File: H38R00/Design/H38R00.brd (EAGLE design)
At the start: 34.6 x 60 mm, 77 parts, among them P1 HEXABIT_17.32_X2_POWER_ONLY, U1 LM5160DNT, U2 TPS65130RGERT, U3 TPS76433DBVT

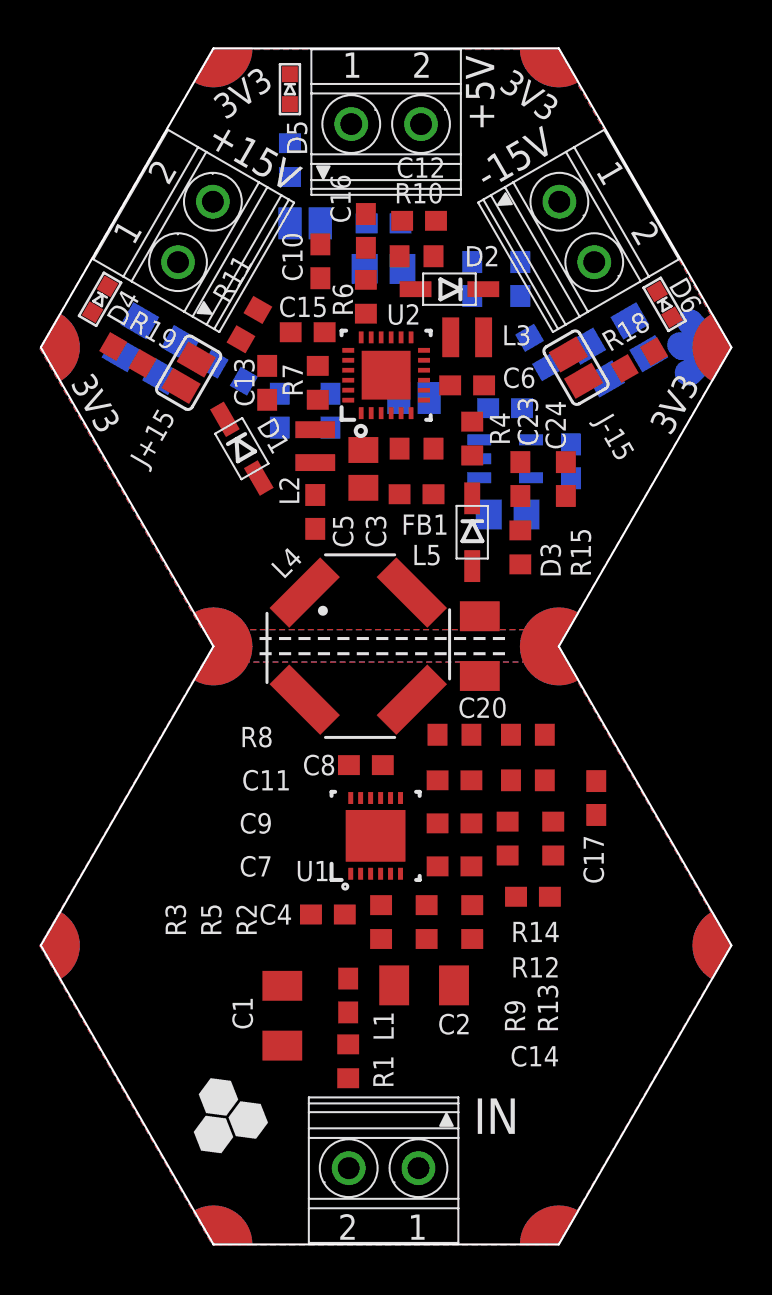
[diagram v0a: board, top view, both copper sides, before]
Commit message: Route most of top layer and raarrange some components
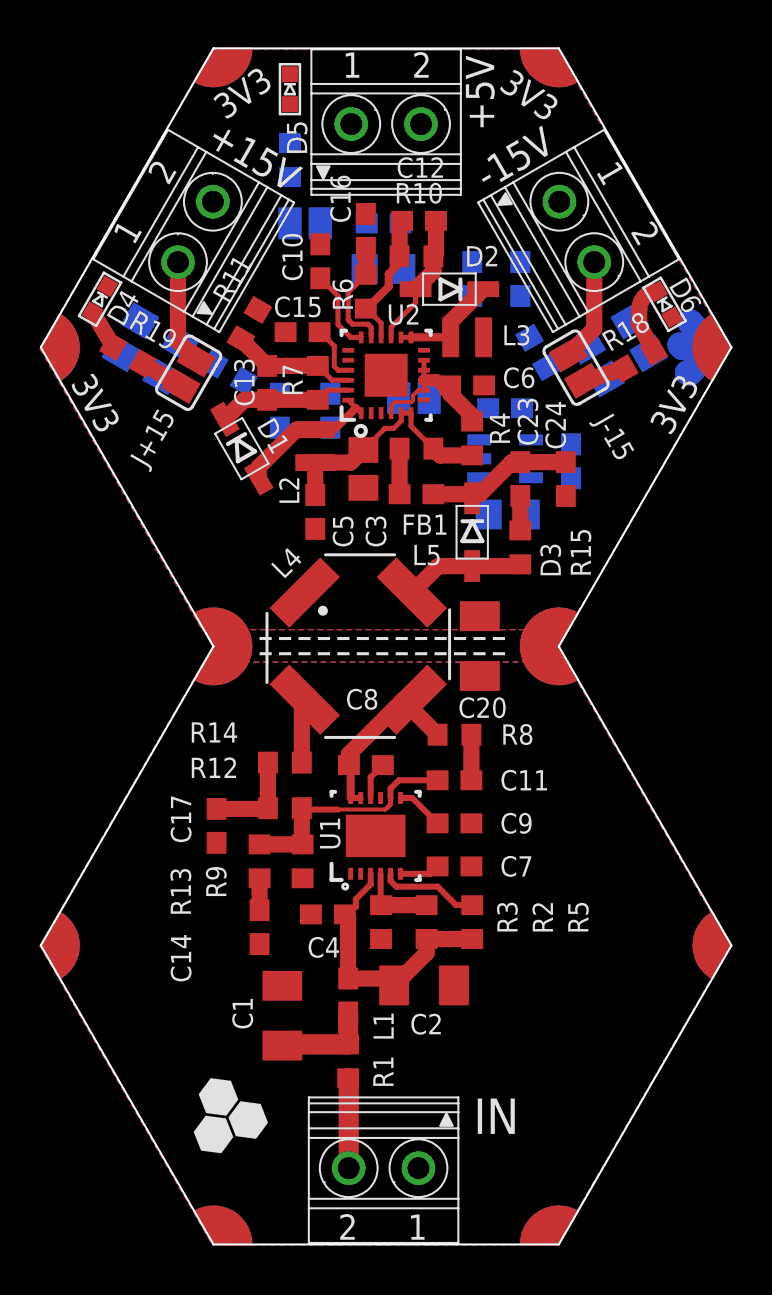
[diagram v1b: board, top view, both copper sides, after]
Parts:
- moved C17 19.1 mm to (24.5, 40.5)
- moved R13 14.8 mm to (26.7, 38.7)
- moved C14 13.8 mm to (26.7, 35.4), turned to 270 degrees
- moved R12 12.3 mm to (27.9, 41.4), turned to 180 degrees
- moved R14 12.3 mm to (27.9, 43.7), turned to 0 degrees
- moved R9 10.4 mm to (28.8, 38.7)
- moved R6 0.25 mm to (32.0, 67.3)
- moved C15 0.25 mm to (28.8, 65.3)
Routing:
- net N$3: track 0.00 -> 13.7 mm
- net N$18: track 0.00 -> 12.0 mm
- net N$10: track 0.00 -> 11.9 mm
- net N$7: track 0.00 -> 9.49 mm
- net N$23: track 0.00 -> 7.86 mm
- net N$15: track 0.00 -> 7.60 mm
- net N$21: track 0.00 -> 7.57 mm
- net N$22: track 0.00 -> 6.79 mm
- net N$27: track 0.00 -> 6.78 mm
- net N$28: track 0.00 -> 6.56 mm
- net N$30: track 0.00 -> 6.25 mm
- net N$16: track 0.00 -> 6.03 mm
- net N$29: track 0.00 -> 5.79 mm
- net N$26: track 0.00 -> 5.58 mm
- net +15V: track 0.00 -> 5.27 mm
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
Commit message: Via stitching. Ready for DRC
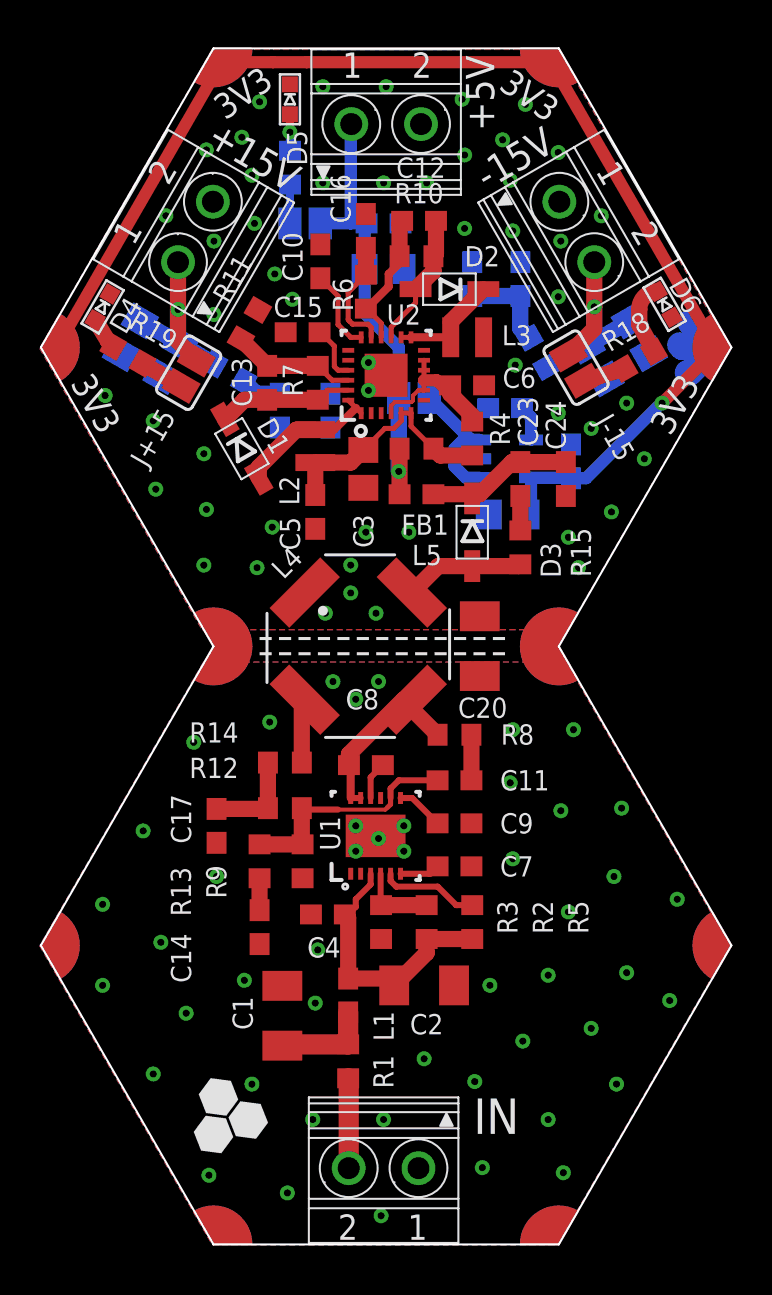
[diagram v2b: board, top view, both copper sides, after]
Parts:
- moved D5 0.51 mm to (28.2, 77.0)
- moved D4 0.40 mm to (18.8, 66.5)
- moved R20 0.38 mm to (28.2, 73.5)
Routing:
- net +3V3: track 0.00 -> 63.5 mm, vias 0 -> 1
- net +5V: track 2.29 -> 22.8 mm, vias 0 -> 1
- net N$36: track 0.00 -> 7.17 mm
- net -15V: track 5.17 -> 12.1 mm, vias 0 -> 1
- net +15V: track 5.27 -> 11.4 mm, vias 0 -> 1
- net N$27: track 6.78 -> 11.5 mm
- net N$22: track 6.79 -> 8.86 mm
- net N$19: track 0.00 -> 1.94 mm
- net N$20: track 0.00 -> 1.83 mm, vias 0 -> 1
- net N$35: track 0.00 -> 1.78 mm
- net IGND: vias 0 -> 50

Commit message: DRC OK
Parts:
- moved C8 0.92 mm to (31.1, 43.8)
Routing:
- net IGND: track 5.58 -> 0.00 mm
- net N$9: track 2.38 -> 6.34 mm, vias 0 -> 2
- net N$22: track 8.86 -> 11.6 mm, vias 0 -> 1
- net N$27: track 11.5 -> 13.9 mm, vias 0 -> 1
- net N$7: track 9.49 -> 11.1 mm
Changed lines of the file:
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@@
 <attribute name="VAULT_REVISION" value="AD34EA21-00F0-458B-A44F-F680A14C5CDA" x="31.623" y="49.53" size="1.778" layer="27" rot="R45" display="off"/>
 </element>
-<element name="C8" library="Hexabitz" package="C-0603" value="10nF" x="32.004" y="43.561" smashed="yes" rot="R180">
-<attribute name="CAPACITANCE" value="10nF" x="32.004" y="43.561" size="1.778" layer="27" rot="R180" display="off"/>
-<attribute name="MFN" value="KEMET" x="32.004" y="43.561" size="1.778" layer="27" rot="R180" display="off"/>
-<attribute name="MPN" value="C0603C103J5RACTU" x="32.004" y="43.561" size="1.778" layer="27" rot="R180" display="off"/>
-<attribute name="NAME" x="30.988" y="46.355" size="1.016" layer="25"/>
-<attribute name="OCTOPART_URL" value="https://octopart.com/c0603c103j5ractu-kemet-91371?r=sp&amp;s=Kyc2xDn-SuWGmNLJldLSIQ" x="32.004" y="43.561" size="1.778" layer="27" rot="R180" display="off"/>
-<attribute name="TOLERANCE" value="10%" x="32.004" y="43.561" size="1.778" layer="27" rot="R180" display="off"/>
-<attribute name="VALUE" x="32.639" y="45.466" size="1.016" layer="27" rot="R180"/>
-<attribute name="VOLTAGE_RATING" value="50V" x="32.004" y="43.561" size="1.778" layer="27" rot="R180" display="off"/>
+<element name="C8" library="Hexabitz" package="C-0603" value="10nF" x="31.115" y="43.815" smashed="yes" rot="R180">
+<attribute name="CAPACITANCE" value="10nF" x="31.115" y="43.815" size="1.778" layer="27" rot="R180" display="off"/>
+<attribute name="MFN" value="KEMET" x="31.115" y="43.815" size="1.778" layer="27" rot="R180" display="off"/>
+<attribute name="MPN" value="C0603C103J5RACTU" x="31.115" y="43.815" size="1.778" layer="27" rot="R180" display="off"/>
+<attribute name="NAME" x="30.099" y="46.609" size="1.016" layer="25"/>
+<attribute name="OCTOPART_URL" value="https://octopart.com/c0603c103j5ractu-kemet-91371?r=sp&amp;s=Kyc2xDn-SuWGmNLJldLSIQ" x="31.115" y="43.815" size="1.778" layer="27" rot="R180" display="off"/>
+<attribute name="TOLERANCE" value="10%" x="31.115" y="43.815" size="1.778" layer="27" rot="R180" display="off"/>
+<attribute name="VALUE" x="31.75" y="45.72" size="1.016" layer="27" rot="R180"/>
+<attribute name="VOLTAGE_RATING" value="50V" x="31.115" y="43.815" size="1.778" layer="27" rot="R180" display="off"/>
 </element>
 <element name="C9" library="Hexabitz" package="C-0603" value="1uF" x="36.449" y="40.64" smashed="yes">
@@
 <vertex x="15.64919375" y="64.4652"/>
 </polygon>
-<polygon width="0.1016" layer="16">
-<vertex x="49.784" y="65.151"/>
-<vertex x="49.784" y="64.262"/>
-<vertex x="49.784" y="63.754"/>
-</polygon>
 <contactref element="P1" pad="PAD_PD12"/>
-<wire x1="49.54" y1="64.516" x2="47.879" y2="64.516" width="1.27" layer="16"/>
-<wire x1="47.879" y1="64.516" x2="47.752" y2="64.643" width="1.27" layer="16"/>
-<wire x1="49.54" y1="64.516" x2="48.27" y2="65.786" width="1.27" layer="16"/>
-<wire x1="48.27" y1="65.786" x2="48.26" y2="65.786" width="1.27" layer="16"/>
-<wire x1="49.54" y1="64.516" x2="48.27" y2="63.246" width="1.27" layer="16"/>
-<wire x1="48.27" y1="63.246" x2="48.133" y2="63.246" width="1.27" layer="16"/>
 <via x="24.003" y="74.422" extent="1-16" drill="0.35"/>
 <via x="25.781" y="75.057" extent="1-16" drill="0.35"/>
@@
 <contactref element="R8" pad="1"/>
 <contactref element="L4" pad="3"/>
-<wire x1="31.242" y1="43.473" x2="31.154" y2="43.561" width="0.8128" layer="1"/>
-<wire x1="31.154" y1="43.561" x2="31.154" y2="44.108" width="0.8128" layer="1"/>
+<wire x1="31.242" y1="42.584" x2="30.265" y2="43.561" width="0.4064" layer="1"/>
+<wire x1="30.265" y1="43.561" x2="30.265" y2="43.815" width="0.4064" layer="1"/>
 <wire x1="33.88899375" y1="46.84299375" x2="34.310003125" y2="46.84299375" width="0.8128" layer="1"/>
-<wire x1="31.154" y1="44.108" x2="33.88899375" y2="46.84299375" width="0.8128" layer="1"/>
-<wire x1="35.599" y1="45.085" x2="33.88899375" y2="46.79500625" width="0.8128" layer="1"/>
-<wire x1="33.88899375" y1="46.79500625" x2="33.88899375" y2="46.84299375" width="0.8128" layer="1"/>
+<wire x1="30.265" y1="44.235" x2="31.72999375" y2="45.69999375" width="0.8128" layer="1"/>
+<wire x1="30.265" y1="43.815" x2="30.265" y2="44.235" width="0.8128" layer="1"/>
 <wire x1="31.742" y1="41.91" x2="31.242" y2="41.91" width="0.3048" layer="1"/>
-<wire x1="31.242" y1="41.91" x2="31.242" y2="43.473" width="0.4064" layer="1"/>
+<wire x1="31.242" y1="41.91" x2="31.242" y2="42.584" width="0.4064" layer="1"/>
+<wire x1="31.72999375" y1="45.69999375" x2="33.167003125" y2="45.69999375" width="0.8128" layer="1"/>
+<wire x1="33.167003125" y1="45.69999375" x2="34.310003125" y2="46.84299375" width="0.8128" layer="1"/>
+<wire x1="34.310003125" y1="46.373996875" x2="34.310003125" y2="46.84299375" width="0.8128" layer="1"/>
+<wire x1="35.599" y1="45.085" x2="34.310003125" y2="46.373996875" width="0.8128" layer="1"/>
 </signal>
 <signal name="N$8">
 <contactref element="U1" pad="10"/>
 <contactref element="C8" pad="1"/>
-<wire x1="32.241996875" y1="41.91" x2="32.241996875" y2="42.948996875" width="0.3048" layer="1"/>
-<wire x1="32.241996875" y1="42.948996875" x2="32.854" y2="43.561" width="0.3048" layer="1"/>
+<wire x1="32.241996875" y1="41.91" x2="32.241996875" y2="43.538003125" width="0.3048" layer="1"/>
+<wire x1="32.241996875" y1="43.538003125" x2="31.965" y2="43.815" width="0.3048" layer="1"/>
 </signal>
 <signal name="N$9">
@@
 <wire x1="33.742" y1="41.91" x2="34.329" y2="41.91" width="0.3048" layer="1"/>
 <wire x1="34.329" y1="41.91" x2="35.599" y2="40.64" width="0.3048" layer="1"/>
-<wire x1="32.742" y1="41.91" x2="33.742" y2="41.91" width="0" layer="19" extent="1-1"/>
+<wire x1="32.742" y1="41.91" x2="32.742" y2="42.775" width="0.254" layer="1"/>
+<wire x1="32.742" y1="42.775" x2="33.528" y2="43.561" width="0.254" layer="1"/>
+<via x="33.528" y="43.561" extent="1-16" drill="0.35"/>
+<wire x1="33.528" y1="43.561" x2="34.329" y2="42.76" width="0.254" layer="16"/>
+<wire x1="34.329" y1="42.76" x2="34.329" y2="41.91" width="0.254" layer="16"/>
+<via x="34.329" y="41.91" extent="1-16" drill="0.35"/>
 </signal>
 <signal name="N$10">
@@
 <wire x1="24.931" y1="60.908240625" x2="25.910759375" y2="61.888" width="0.8128" layer="1"/>
 <wire x1="25.910759375" y1="61.888" x2="27.051" y2="61.888" width="0.8128" layer="1"/>
-<wire x1="27.051" y1="61.888" x2="29.591" y2="61.888" width="0.8128" layer="1"/>
+<wire x1="29.337" y1="62.142" x2="28.575" y2="62.142" width="0.8128" layer="1"/>
+<wire x1="28.575" y1="62.142" x2="27.305" y2="62.142" width="0.8128" layer="1"/>
+<wire x1="27.051" y1="61.888" x2="27.305" y2="62.142" width="0.8128" layer="1"/>
+<wire x1="29.337" y1="62.142" x2="29.591" y2="61.888" width="0.8128" layer="1"/>
 <wire x1="31.12" y1="62.369" x2="30.072" y2="62.369" width="0.254" layer="1"/>
 <wire x1="30.072" y1="62.369" x2="29.591" y2="61.888" width="0.254" layer="1"/>
 <wire x1="25.882121875" y1="62.821" x2="26.512121875" y2="62.191" width="0.8128" layer="16"/>
 <wire x1="26.512121875" y1="62.191" x2="27.686" y2="62.191" width="0.8128" layer="16"/>
-<wire x1="30.072" y1="62.369" x2="30.226" y2="62.191" width="0" layer="19" extent="1-16"/>
-<wire x1="26.512121875" y1="62.191" x2="27.051" y2="61.888" width="0" layer="19" extent="1-16"/>
+<wire x1="27.686" y1="62.191" x2="28.526" y2="62.191" width="0.8128" layer="16"/>
+<wire x1="28.526" y1="62.191" x2="28.575" y2="62.142" width="0.8128" layer="16"/>
+<via x="28.575" y="62.142" extent="1-16" drill="0.35"/>
+<wire x1="28.575" y1="62.142" x2="30.177" y2="62.142" width="0.8128" layer="16"/>
+<wire x1="30.177" y1="62.142" x2="30.226" y2="62.191" width="0.8128" layer="16"/>
 </signal>
 <signal name="N$23">
@@
 <wire x1="39.751" y1="67.095" x2="39.751" y2="65.46211875" width="0.8128" layer="16"/>
 <wire x1="39.751" y1="65.46211875" x2="40.215" y2="64.99811875" width="0.8128" layer="16"/>
-<wire x1="35.394" y1="68.336" x2="37.338" y2="67.095" width="0" layer="19" extent="1-16"/>
+<wire x1="37.338" y1="67.095" x2="36.635" y2="67.095" width="0.6096" layer="16"/>
+<wire x1="36.635" y1="67.095" x2="35.394" y2="68.336" width="0.6096" layer="16"/>
+<via x="35.394" y="68.336" extent="1-16" drill="0.35"/>
 </signal>
 <signal name="+5V">
@@
 <contactref element="FB1" pad="1"/>
 <contactref element="J3V3" pad="2"/>
-<wire x1="33.694" y1="59.436" x2="33.694" y2="57.15" width="0.8128" layer="1"/>
 <wire x1="33.655" y1="61.976" x2="33.655" y2="64.516" width="0.6096" layer="16"/>
 <wire x1="31.943" y1="66.228" x2="31.943" y2="68.453" width="0.6096" layer="16"/>
@@
 <wire x1="33.655" y1="61.976" x2="33.655" y2="58.293" width="0.8128" layer="16"/>
 <via x="33.655" y="58.293" extent="1-16" drill="0.35"/>
-<wire x1="33.655" y1="58.293" x2="33.694" y2="59.436" width="0" layer="19" extent="1-16"/>
+<wire x1="33.694" y1="57.15" x2="33.694" y2="58.254" width="0.8128" layer="1"/>
+<wire x1="33.694" y1="58.254" x2="33.655" y2="58.293" width="0.8128" layer="1"/>
+<wire x1="33.655" y1="58.293" x2="33.655" y2="59.397" width="0.8128" layer="1"/>
+<wire x1="33.655" y1="59.397" x2="33.694" y2="59.436" width="0.8128" layer="1"/>
 </signal>
 <signal name="+15V">
@@
 <wire x1="33.694" y1="69.088" x2="33.694" y2="68.746" width="0.4064" layer="1"/>
 <wire x1="33.694" y1="68.746" x2="33.147" y2="68.199" width="0.4064" layer="1"/>
-<wire x1="32.77" y1="65.019" x2="32.77" y2="65.733" width="0.254" layer="1"/>
-<wire x1="32.77" y1="65.733" x2="32.297" y2="66.206" width="0.254" layer="1"/>
-<wire x1="32.297" y1="66.206" x2="32.043" y2="66.46" width="0" layer="19" extent="1-1"/>
+<wire x1="32.77" y1="65.821" x2="32.131" y2="66.46" width="0.254" layer="1"/>
+<wire x1="32.004" y1="66.46" x2="32.131" y2="66.46" width="0.254" layer="1"/>
+<wire x1="32.77" y1="65.019" x2="32.77" y2="65.821" width="0.254" layer="1"/>
 </signal>
 <signal name="N$29">
@@
 <mfgpreviewcolor name="substratecolor" color="0xFF786E46"/>
 </mfgpreviewcolors>
+<errors>
+</errors>
 </board>
 </drawing>
